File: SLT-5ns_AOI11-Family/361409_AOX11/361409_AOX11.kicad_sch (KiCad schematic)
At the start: 11 parts, among them U1 12-Pin_SLx_Can

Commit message: Updated schematics
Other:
- note removed: "B"
- note removed: "C"
- note removed: "E"
- note removed: "Transistor Die Layout (top view)"
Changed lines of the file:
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@@
     (stroke (width 0) (type default) (color 0 0 0 0))
-  )
-  (polyline (pts (xy 252.73 29.21) (xy 252.73 40.64))
-    (stroke (width 0) (type solid) (color 0 0 0 0))
   )
   (wire (pts (xy 139.7 115.57) (xy 148.59 115.57))
     (stroke (width 0) (type default) (color 0 0 0 0))
-  )
-  (polyline (pts (xy 264.16 40.64) (xy 252.73 40.64))
-    (stroke (width 0) (type solid) (color 0 0 0 0))
   )
   (wire (pts (xy 139.7 104.14) (xy 148.59 104.14))
@@
   (wire (pts (xy 156.21 92.71) (xy 165.1 92.71))
     (stroke (width 0) (type default) (color 0 0 0 0))
-  )
-  (polyline (pts (xy 252.73 29.21) (xy 264.16 29.21))
-    (stroke (width 0) (type solid) (color 0 0 0 0))
   )
   (wire (pts (xy 101.6 127) (xy 110.49 127))
@@
   (wire (pts (xy 139.7 92.71) (xy 148.59 92.71))
     (stroke (width 0) (type default) (color 0 0 0 0))
-  )
-  (polyline (pts (xy 264.16 29.21) (xy 264.16 40.64))
-    (stroke (width 0) (type solid) (color 0 0 0 0))
   )
   (wire (pts (xy 156.21 104.14) (xy 165.1 104.14))
@@
     (stroke (width 0) (type default) (color 0 0 0 0))
   )
-  (text "C" (at 257.81 39.37 0)
-    (effects (font (size 1.27 1.27)) (justify left bottom))
-  )
   (text "DC" (at 120.65 99.06 0)
     (effects (font (size 1.27 1.27)) (justify left bottom))
@@
     (effects (font (size 1.27 1.27)) (justify left bottom))
   )
-  (text "E" (at 254 33.02 0)
-    (effects (font (size 1.27 1.27)) (justify left bottom))
-  )
   (text "DB" (at 158.75 121.92 0)
     (effects (font (size 1.27 1.27)) (justify left bottom))
@@
     (effects (font (size 1.27 1.27)) (justify left bottom))
   )
-  (text "B" (at 261.62 33.02 0)
-    (effects (font (size 1.27 1.27)) (justify left bottom))
-  )
-  (text "Transistor Die Layout (top view)" (at 243.84 27.94 0)
-    (effects (font (size 1.27 1.27)) (justify left bottom))
-  )

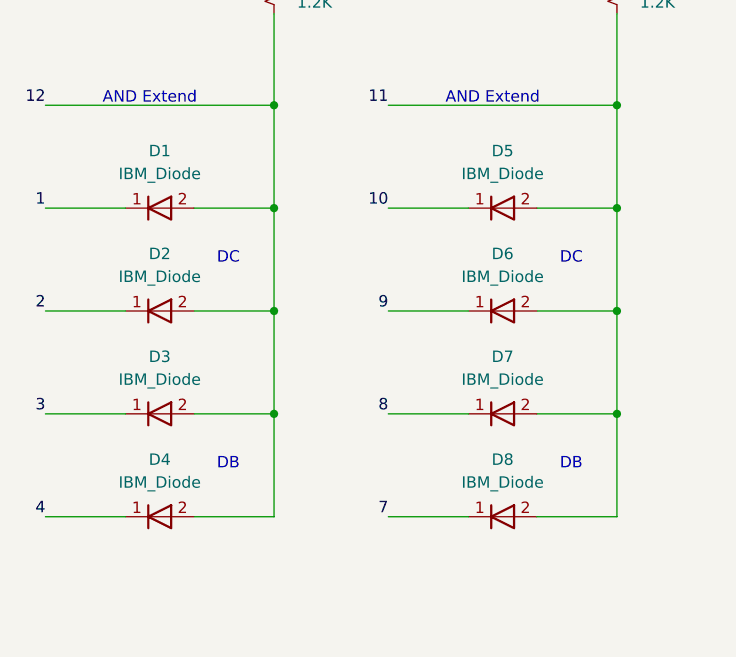
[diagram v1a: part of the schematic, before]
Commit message: Finished off the SLT-30 family of parts, started on the SLT-700 family. Changed labeling of transistors and diodes in all schematics, but have yet to update all the pdf files. This is a TODO...
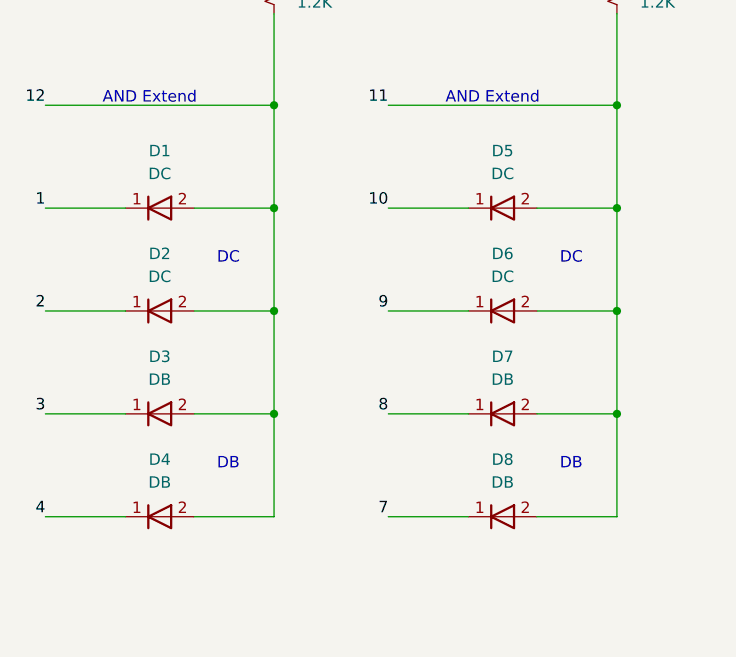
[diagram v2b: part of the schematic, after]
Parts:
- D1, D2, D5, D6: value IBM_Diode -> DC
- D3, D4, D7, D8: value IBM_Diode -> DB
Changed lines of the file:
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@@
     (in_bom yes) (on_board yes) (fields_autoplaced)
     (property "Reference" "D4" (id 0) (at 114.3 120.65 0))
-    (property "Value" "IBM_Diode" (id 1) (at 114.3 123.19 0))
+    (property "Value" "DB" (id 1) (at 114.3 123.19 0))
     (property "Footprint" "Diode_SMD:D_0201_0603Metric" (id 2) (at 114.3 124.46 0)
       (effects (font (size 1.27 1.27)) hide)
@@
     (in_bom yes) (on_board yes) (fields_autoplaced)
     (property "Reference" "D2" (id 0) (at 114.3 97.79 0))
-    (property "Value" "IBM_Diode" (id 1) (at 114.3 100.33 0))
+    (property "Value" "DC" (id 1) (at 114.3 100.33 0))
     (property "Footprint" "Diode_SMD:D_0201_0603Metric" (id 2) (at 114.3 101.6 0)
       (effects (font (size 1.27 1.27)) hide)
@@
     (in_bom yes) (on_board yes) (fields_autoplaced)
     (property "Reference" "D7" (id 0) (at 152.4 109.22 0))
-    (property "Value" "IBM_Diode" (id 1) (at 152.4 111.76 0))
+    (property "Value" "DB" (id 1) (at 152.4 111.76 0))
     (property "Footprint" "Diode_SMD:D_0201_0603Metric" (id 2) (at 152.4 113.03 0)
       (effects (font (size 1.27 1.27)) hide)
@@
     (in_bom yes) (on_board yes) (fields_autoplaced)
     (property "Reference" "D1" (id 0) (at 114.3 86.36 0))
-    (property "Value" "IBM_Diode" (id 1) (at 114.3 88.9 0))
+    (property "Value" "DC" (id 1) (at 114.3 88.9 0))
     (property "Footprint" "Diode_SMD:D_0201_0603Metric" (id 2) (at 114.3 90.17 0)
       (effects (font (size 1.27 1.27)) hide)
@@
     (in_bom yes) (on_board yes) (fields_autoplaced)
     (property "Reference" "D8" (id 0) (at 152.4 120.65 0))
-    (property "Value" "IBM_Diode" (id 1) (at 152.4 123.19 0))
+    (property "Value" "DB" (id 1) (at 152.4 123.19 0))
     (property "Footprint" "Diode_SMD:D_0201_0603Metric" (id 2) (at 152.4 124.46 0)
       (effects (font (size 1.27 1.27)) hide)
@@
     (in_bom yes) (on_board yes) (fields_autoplaced)
     (property "Reference" "D3" (id 0) (at 114.3 109.22 0))
-    (property "Value" "IBM_Diode" (id 1) (at 114.3 111.76 0))
+    (property "Value" "DB" (id 1) (at 114.3 111.76 0))
     (property "Footprint" "Diode_SMD:D_0201_0603Metric" (id 2) (at 114.3 113.03 0)
       (effects (font (size 1.27 1.27)) hide)
@@
     (in_bom yes) (on_board yes) (fields_autoplaced)
     (property "Reference" "D5" (id 0) (at 152.4 86.36 0))
-    (property "Value" "IBM_Diode" (id 1) (at 152.4 88.9 0))
+    (property "Value" "DC" (id 1) (at 152.4 88.9 0))
     (property "Footprint" "Diode_SMD:D_0201_0603Metric" (id 2) (at 152.4 90.17 0)
       (effects (font (size 1.27 1.27)) hide)
@@
     (in_bom yes) (on_board yes) (fields_autoplaced)
     (property "Reference" "D6" (id 0) (at 152.4 97.79 0))
-    (property "Value" "IBM_Diode" (id 1) (at 152.4 100.33 0))
+    (property "Value" "DC" (id 1) (at 152.4 100.33 0))
     (property "Footprint" "Diode_SMD:D_0201_0603Metric" (id 2) (at 152.4 101.6 0)
       (effects (font (size 1.27 1.27)) hide)
@@
   (symbol_instances
     (path "/801d24ff-be6b-468d-a51b-7691568aa1d6"
-      (reference "D1") (unit 1) (value "IBM_Diode") (footprint "Diode_SMD:D_0201_0603Metric")
+      (reference "D1") (unit 1) (value "DC") (footprint "Diode_SMD:D_0201_0603Metric")
     )
     (path "/15a433c4-0335-46e4-884c-814357806383"
-      (reference "D2") (unit 1) (value "IBM_Diode") (footprint "Diode_SMD:D_0201_0603Metric")
+      (reference "D2") (unit 1) (value "DC") (footprint "Diode_SMD:D_0201_0603Metric")
     )
     (path "/b60d9340-c16c-48dd-8b20-3b5943f6c8ab"
-      (reference "D3") (unit 1) (value "IBM_Diode") (footprint "Diode_SMD:D_0201_0603Metric")
+      (reference "D3") (unit 1) (value "DB") (footprint "Diode_SMD:D_0201_0603Metric")
     )
     (path "/096216c5-6902-43a5-8004-8a4114c8baa4"
-      (reference "D4") (unit 1) (value "IBM_Diode") (footprint "Diode_SMD:D_0201_0603Metric")
+      (reference "D4") (unit 1) (value "DB") (footprint "Diode_SMD:D_0201_0603Metric")
     )
     (path "/e1f12525-18b0-44bc-a18d-820be7b9946e"
-      (reference "D5") (unit 1) (value "IBM_Diode") (footprint "Diode_SMD:D_0201_0603Metric")
+      (reference "D5") (unit 1) (value "DC") (footprint "Diode_SMD:D_0201_0603Metric")
     )
     (path "/e5207290-41d1-4708-be96-2b2603b0ffee"
-      (reference "D6") (unit 1) (value "IBM_Diode") (footprint "Diode_SMD:D_0201_0603Metric")
+      (reference "D6") (unit 1) (value "DC") (footprint "Diode_SMD:D_0201_0603Metric")
     )
     (path "/1be5506a-07a3-447d-b379-4e04e402bbb9"
-      (reference "D7") (unit 1) (value "IBM_Diode") (footprint "Diode_SMD:D_0201_0603Metric")
+      (reference "D7") (unit 1) (value "DB") (footprint "Diode_SMD:D_0201_0603Metric")
     )
     (path "/8e4b9e6c-d9b9-437f-9616-3123e2a2c38e"
-      (reference "D8") (unit 1) (value "IBM_Diode") (footprint "Diode_SMD:D_0201_0603Metric")
+      (reference "D8") (unit 1) (value "DB") (footprint "Diode_SMD:D_0201_0603Metric")
     )
     (path "/512fd277-9de7-454a-b3d9-ab06f52cae1a"
